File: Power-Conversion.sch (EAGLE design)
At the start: 42 parts, among them Q1 SUM90P10-19L, U7 LM2678

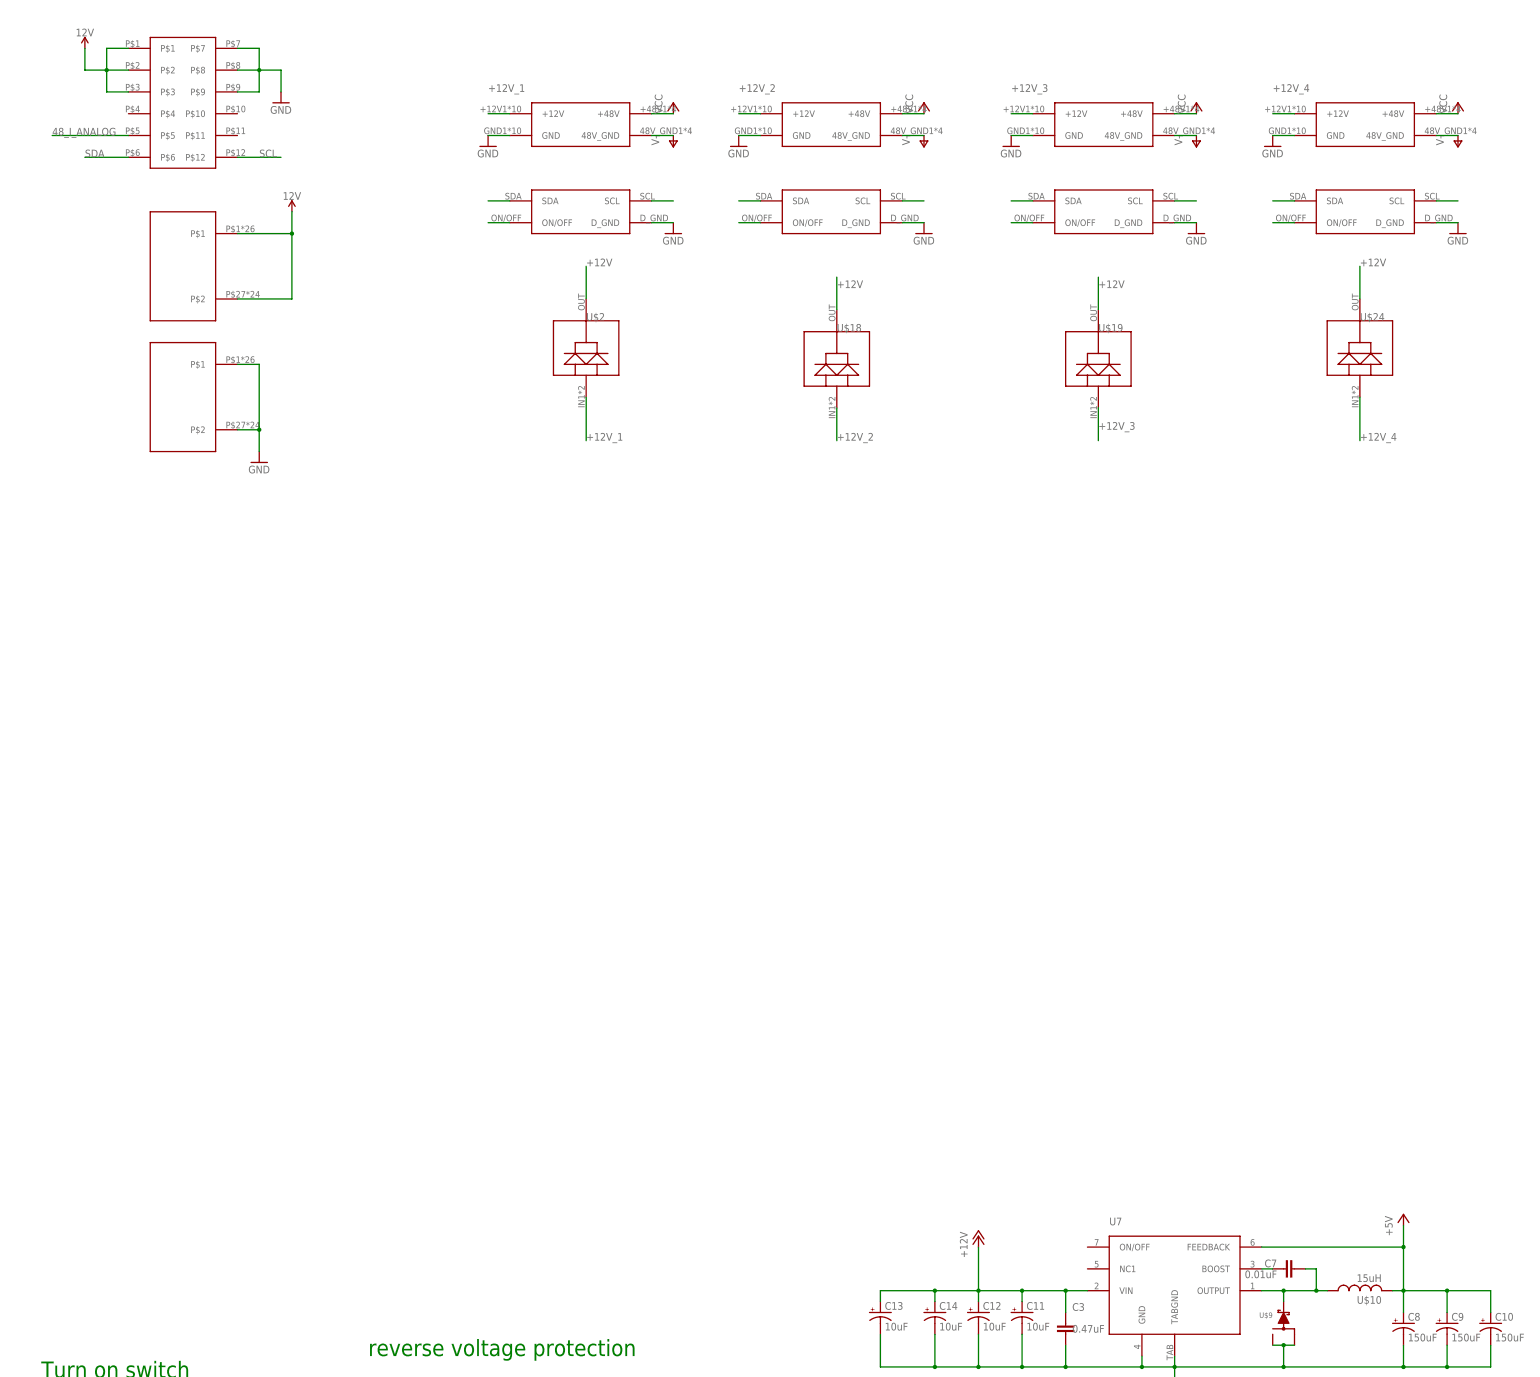
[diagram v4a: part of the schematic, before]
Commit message: Initial layout of parts has begun.  Still need to reduce down the size a lot...
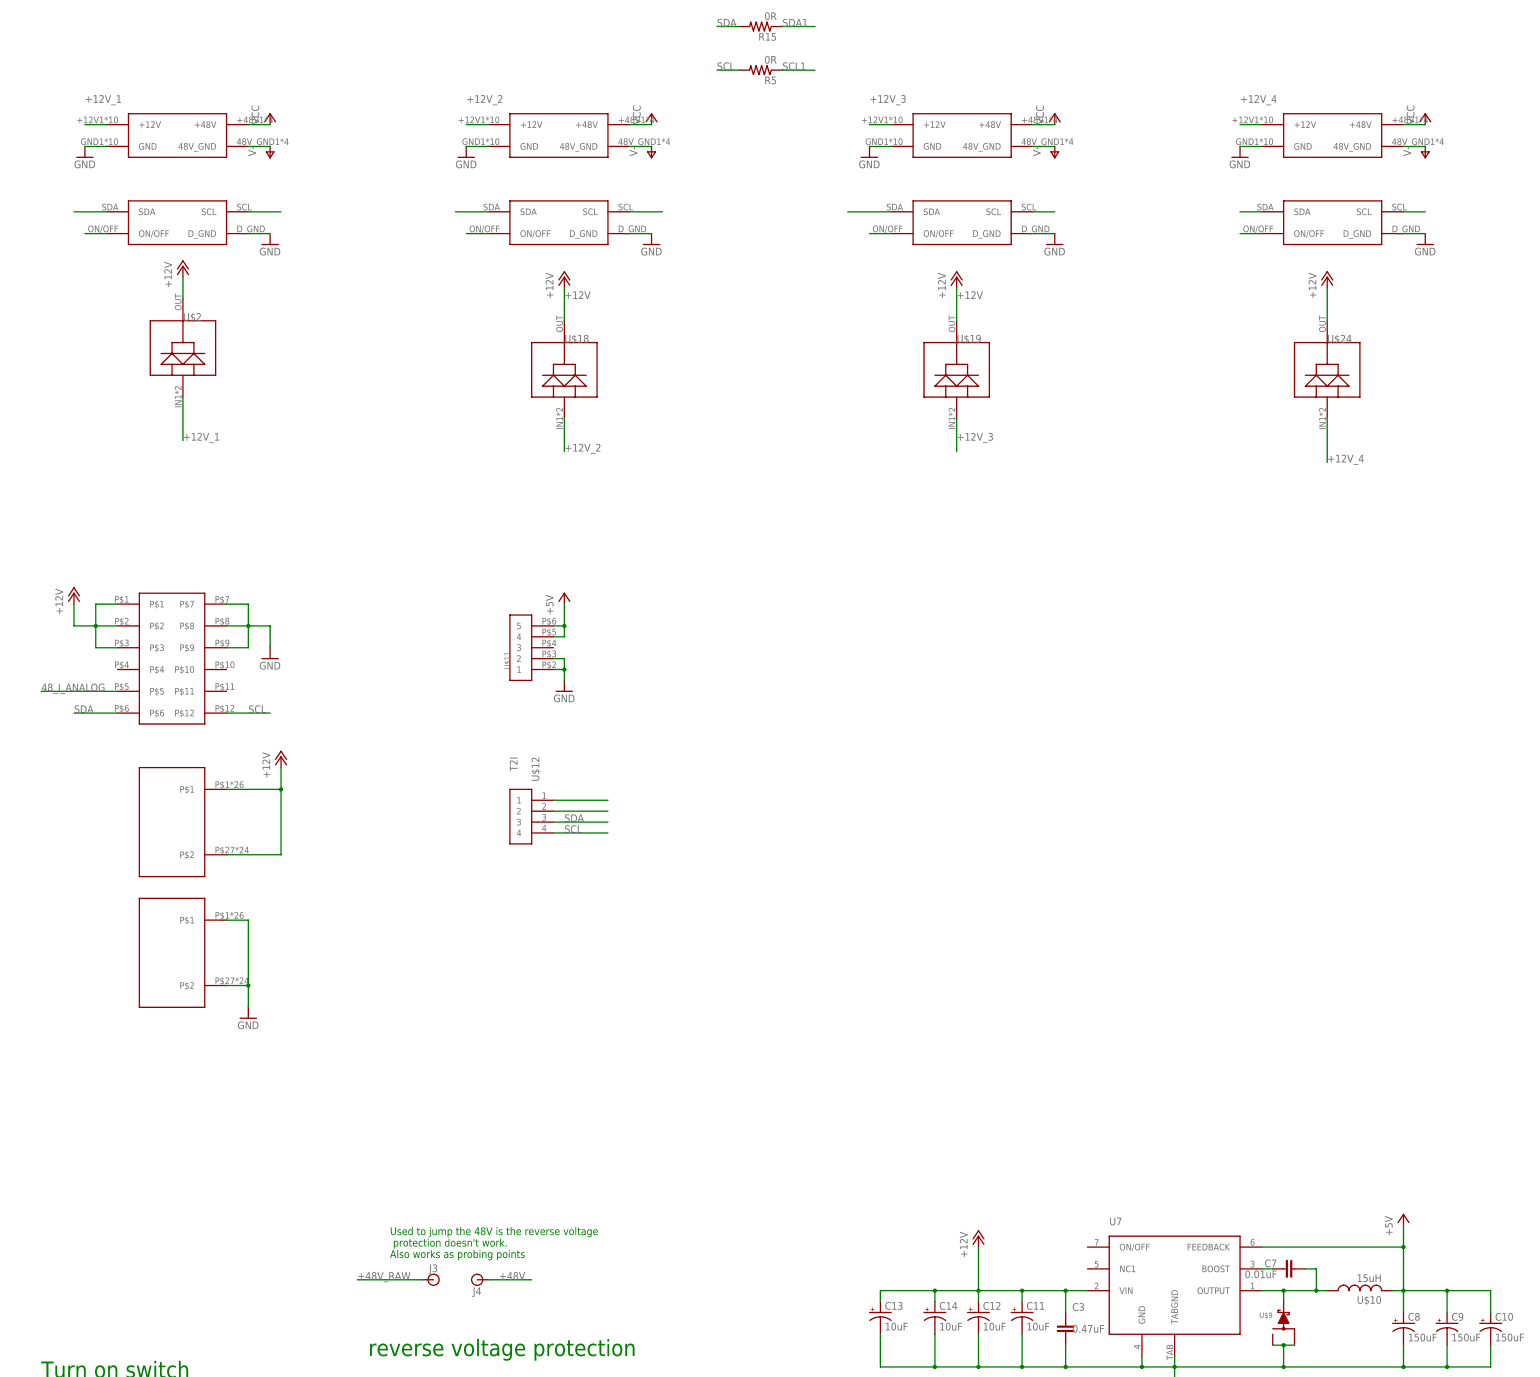
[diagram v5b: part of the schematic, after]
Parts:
- added J3, J4: (no value), SparkFun-Connectors:BANANA_CONN
- added R15, R5: 0R, resistor:R-US_R0603
- added U$11: T2I5P, BackplaneParts:T2I5P
- added U$12: T2I, BackplaneParts:T2I
- U$24: SPICEPREFIX (none) -> B
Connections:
- removed net 12V: U$16.P$1, U$16.P$2, U$16.P$3, U$8.P$1, U$8.P$2
- new net N$2: U$12.1
- new net N$3: U$12.2
- new net SCL1: R5.1, U$20.SCL, U$21.SCL, U$22.SCL
- new net SCL4: U$23.SCL
- new net SDA1: R15.1, U$20.SDA, U$21.SDA, U$22.SDA
- new net SDA4: U$23.SDA
- net +12V: now also U$16.P$1, U$16.P$2, U$16.P$3, U$8.P$1, U$8.P$2
- net +48V: now also J4.1
- net +48V_RAW: now also J3.1
- net +5V: now also U$11.4, U$11.5
- net GND: now also U$11.1, U$11.2
- net SCL: now also R5.2, U$12.4; no longer U$20.SCL, U$21.SCL, U$22.SCL, U$23.SCL
- net SDA: now also R15.2, U$12.3; no longer U$20.SDA, U$21.SDA, U$22.SDA, U$23.SDA
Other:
- note added: "Used to jump the 48V is the reverse voltage protection doesn't work. Also works as probing points"
- moved on the sheet: U$18, U$19, U$2, U$24

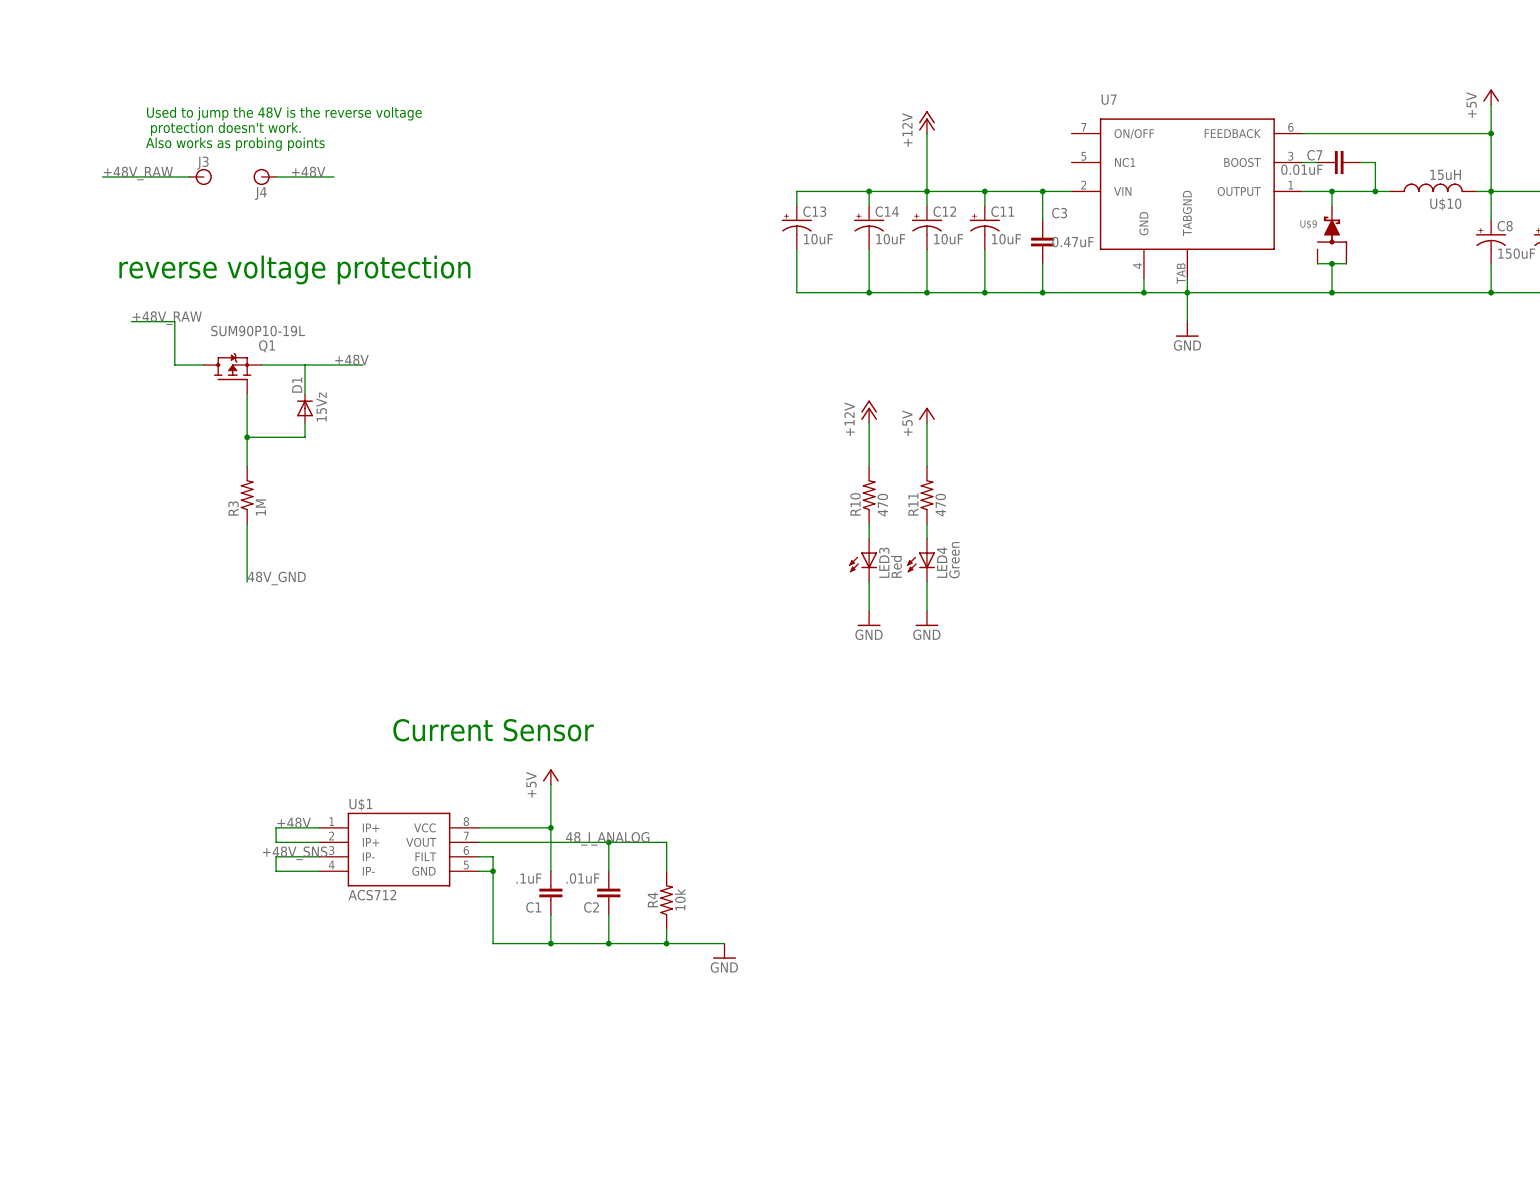
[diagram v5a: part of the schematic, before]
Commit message: Shrinking down the board more and figuring out part placement
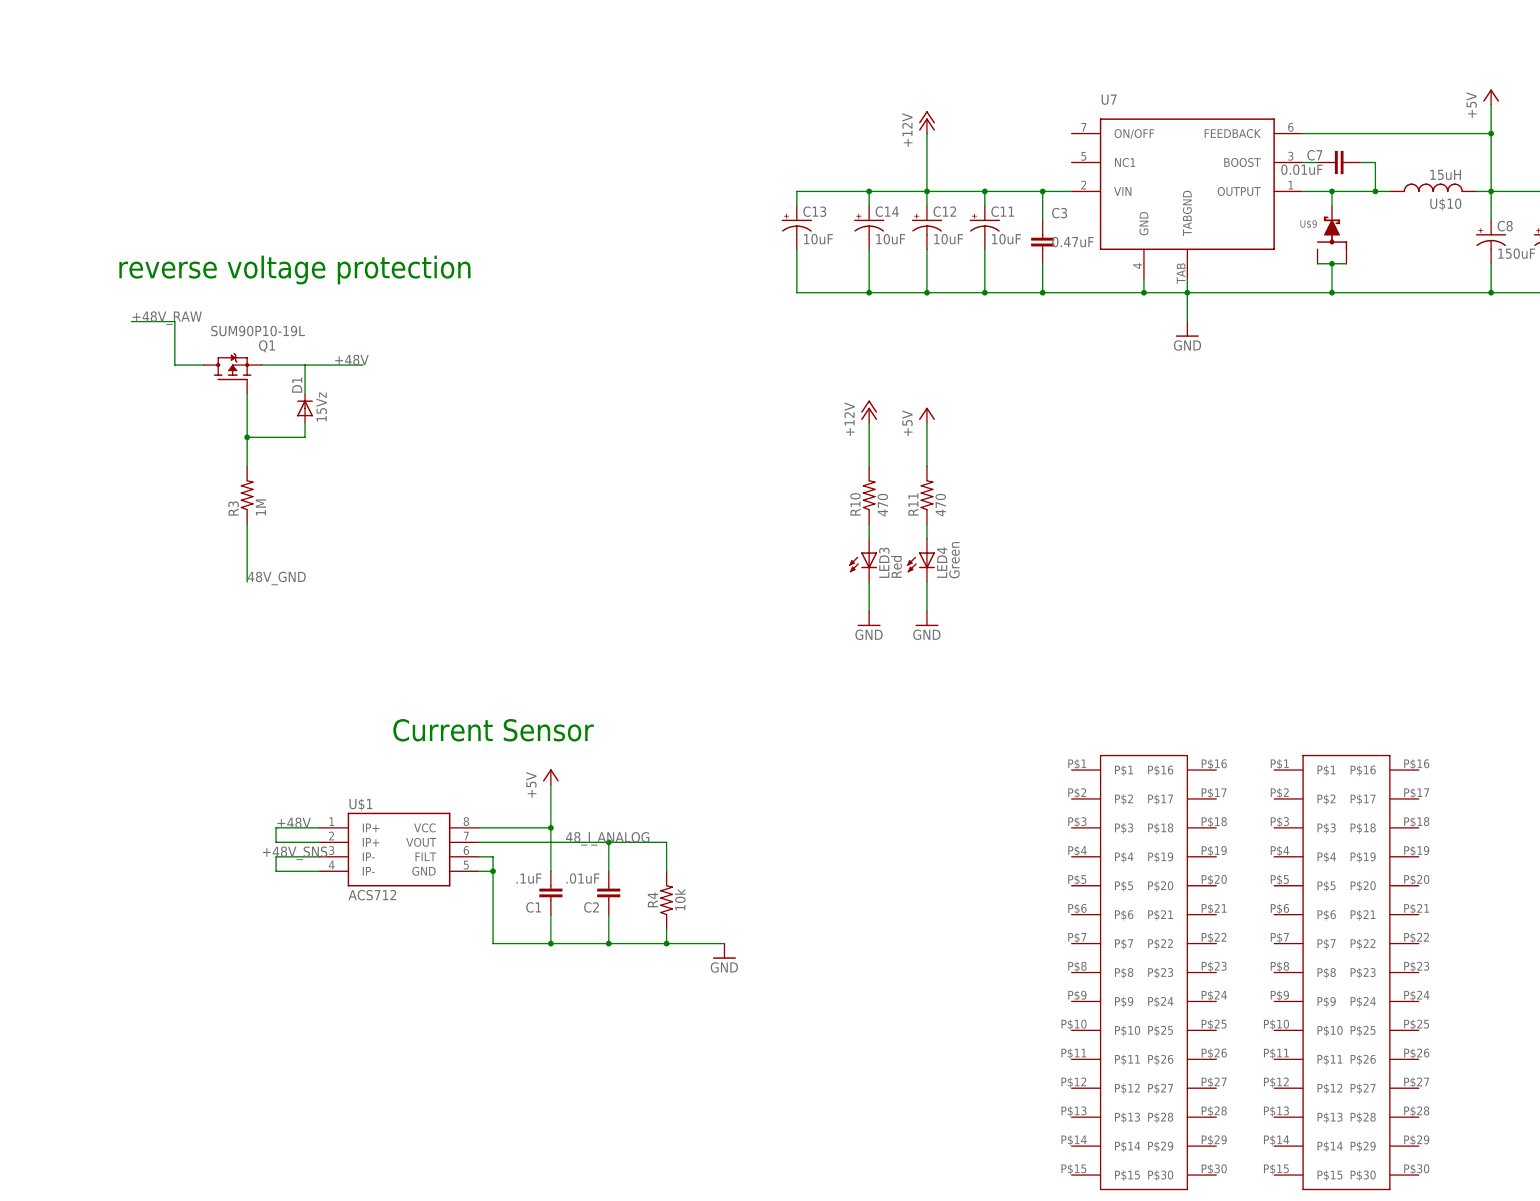
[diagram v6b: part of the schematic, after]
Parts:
- removed J3, J4: (no value), SparkFun-Connectors:BANANA_CONN
- added U$13, U$14: POWER_BRICK_CONNECTORS(2X15), MotherBoardParts2:POWER_BRICK_CONNECTORS(2X15)
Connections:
- net +48V: no longer J4.1
- net +48V_RAW: no longer J3.1
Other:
- note removed: "Used to jump the 48V is the reverse voltage protection doesn't work. Also works as probing points"
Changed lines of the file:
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@@
 <part name="GND7" library="supply1" deviceset="GND" device=""/>
 <part name="P+16" library="supply1" deviceset="+5V" device=""/>
-<part name="J3" library="SparkFun-Connectors" deviceset="BANANA_CONN" device=""/>
-<part name="J4" library="SparkFun-Connectors" deviceset="BANANA_CONN" device=""/>
+<part name="U$13" library="MotherBoardParts2" deviceset="POWER_BRICK_CONNECTORS(2X15)" device=""/>
+<part name="U$14" library="MotherBoardParts2" deviceset="POWER_BRICK_CONNECTORS(2X15)" device=""/>
 </parts>
 <sheets>
@@
 <text x="12.7" y="114.3" size="2.54" layer="91">48 VOLT CONNECTOR</text>
 <text x="144.78" y="129.54" size="3.81" layer="91">Current Sensor</text>
-<text x="101.6" y="233.68" size="1.778" layer="91">Used to jump the 48V is the reverse voltage
- protection doesn't work.
-Also works as probing points</text>
 </plain>
 <instances>
@@
 <instance part="GND7" gate="1" x="142.24" y="365.76"/>
 <instance part="P+16" gate="1" x="142.24" y="388.62"/>
-<instance part="J3" gate="G$1" x="111.76" y="228.6"/>
-<instance part="J4" gate="G$1" x="121.92" y="228.6" rot="R180"/>
+<instance part="U$13" gate="G$1" x="276.86" y="91.44"/>
+<instance part="U$14" gate="G$1" x="312.42" y="91.44"/>
 </instances>
 <busses>
@@
 <label x="124.46" y="114.3" size="1.778" layer="95"/>
 </segment>
-<segment>
-<pinref part="J4" gate="G$1" pin="1"/>
-<wire x1="124.46" y1="228.6" x2="134.62" y2="228.6" width="0.1524" layer="91"/>
-<label x="127" y="228.6" size="1.778" layer="95"/>
-</segment>
 </net>
 <net name="48V_GND" class="0">
@@
 <label x="20.32" y="104.14" size="1.778" layer="95"/>
 </segment>
-<segment>
-<pinref part="J3" gate="G$1" pin="1"/>
-<wire x1="109.22" y1="228.6" x2="93.98" y2="228.6" width="0.1524" layer="91"/>
-<label x="93.98" y="228.6" size="1.778" layer="95"/>
-</segment>
 </net>
 <net name="SCL" class="0">
@@
 </drawing>
 <compatibility>
-<note version="6.3" minversion="6.2.2" severity="warning">
-Since Version 6.2.2 text objects can contain more than one line,
-which will not be processed correctly with this version.
-</note>
 <note version="8.2" severity="warning">
 Since Version 8.2, EAGLE supports online libraries. The ids
